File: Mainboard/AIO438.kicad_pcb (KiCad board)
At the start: 4 copper layers, 121 x 60 mm, 163 parts, among them J1 JST-PH 01x03, J10 U.FL, J11 JST-PH 01x02, J2 JST-PH 01x10, J3 PinHeader 02x03, J4 5mm screwterminal 01x12, J5 JST-PH 01x02, J6 JST-PH 01x02, J7 PinHeader 01x06, J8 USB_B_Micro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

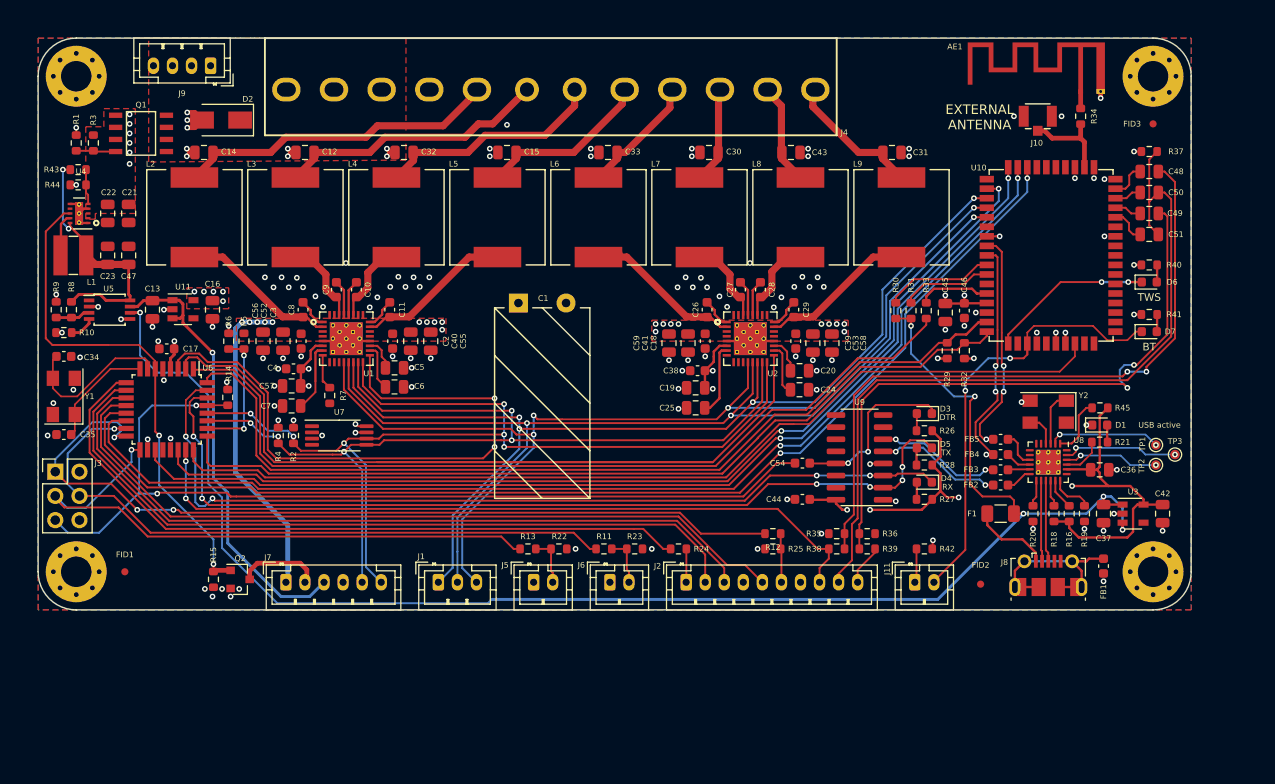
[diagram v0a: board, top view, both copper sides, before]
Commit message: Modify library references
As described in the README of the newly added libraries submodule.
Schematic and PCB are synced.

Hardware folder is renamed to mainboard
Any other PCBs can be put in their own subfolder in the gitrepo

Commit also swaps source/drain of Q1 because it appeared wrong for some
reason after updating all symbol/footprints.
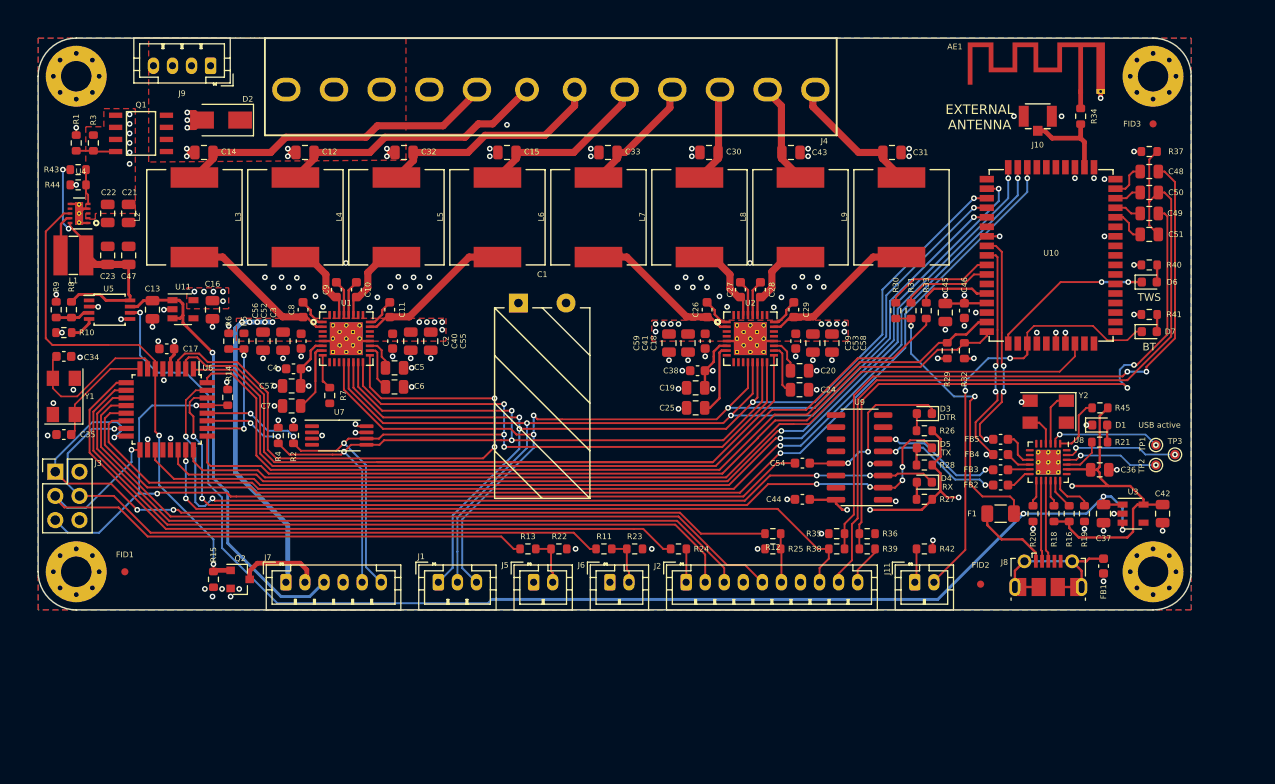
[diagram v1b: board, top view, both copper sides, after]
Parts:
- C1: footprint ZOUDIOfootprints:Cap_Rad_D10_P5_horizontal -> ZOUDIO-footprints:Cap_Rad_D10_P5_horizontal
- J10: footprint ZOUDIOfootprints:Hirose_U.FL-R-SMT-1 -> ZOUDIO-footprints:Hirose_U.FL-R-SMT-1
- J4: footprint ZOUDIOfootprints:Multicomp_12P_5mm -> ZOUDIO-footprints:Multicomp_12P_5mm
- L1: footprint ZOUDIOfootprints:SRN4012TA -> ZOUDIO-footprints:SRN4012TA
- L2, L3, L4, L5, L6, L7, L8, L9: footprint ZOUDIOfootprints:Murata_1274AS-H-100M -> ZOUDIO-footprints:Murata_1274AS-H-100M
- LOGO1: footprint ZOUDIOfootprints:ZOUDIO25mm -> ZOUDIO-footprints:ZOUDIO25mm
- Q1: footprint ZOUDIOfootprints:SOIC8_mosfet -> ZOUDIO-footprints:SOIC8_mosfet
- U1, U2: footprint ZOUDIOfootprints:TAS5825M -> ZOUDIO-footprints:TAS5825M
- U10: footprint ZOUDIOfootprints:BTM331 -> ZOUDIO-footprints:BTM331

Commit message: Add USB-C
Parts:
- removed J8: USB_B_Micro, Connector_USB:USB_Micro-B_Molex-105017-0001
- added P1: USB_C_Plug_USB2.0, Connector_USB:USB_C_Receptacle_Palconn_UTC16-G, F.Cu at (208.7, 128.0)

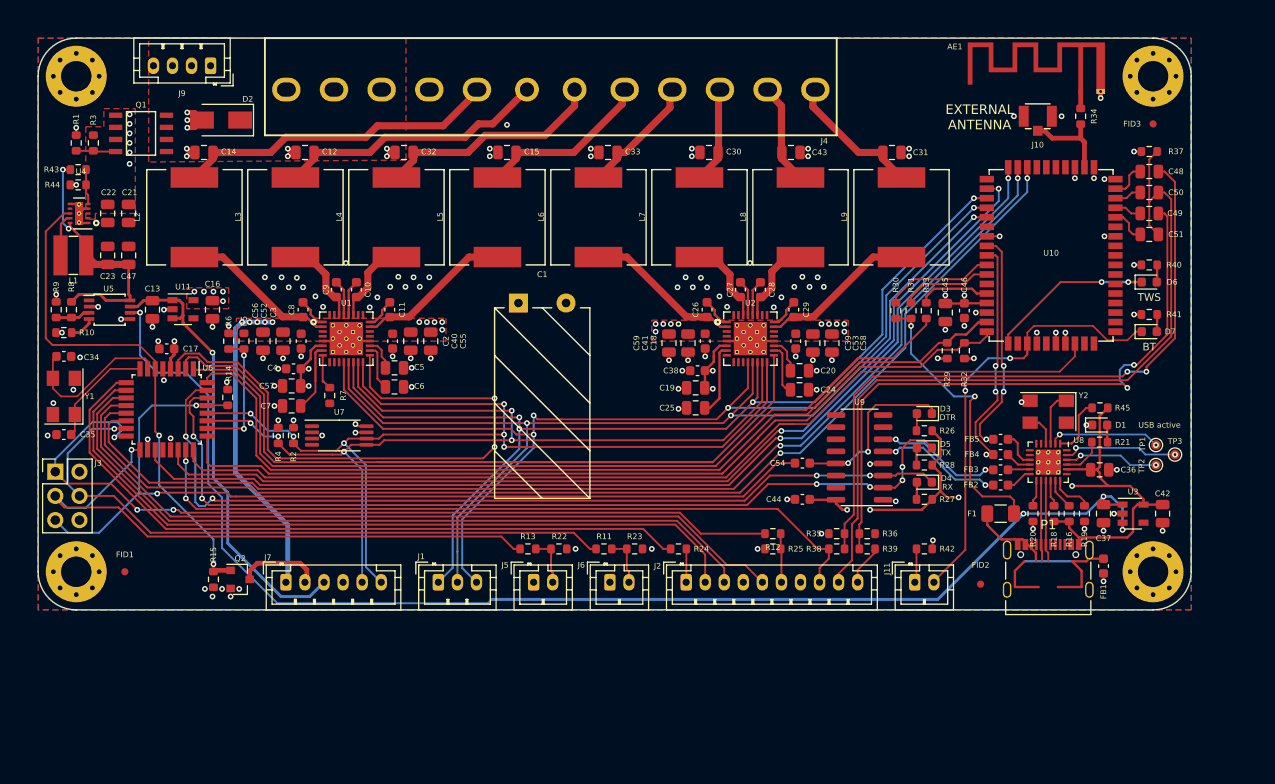
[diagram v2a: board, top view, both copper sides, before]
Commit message: Before testing CH340B and VCHG
Cleaned up amp lay-out a bit in the meanwhile
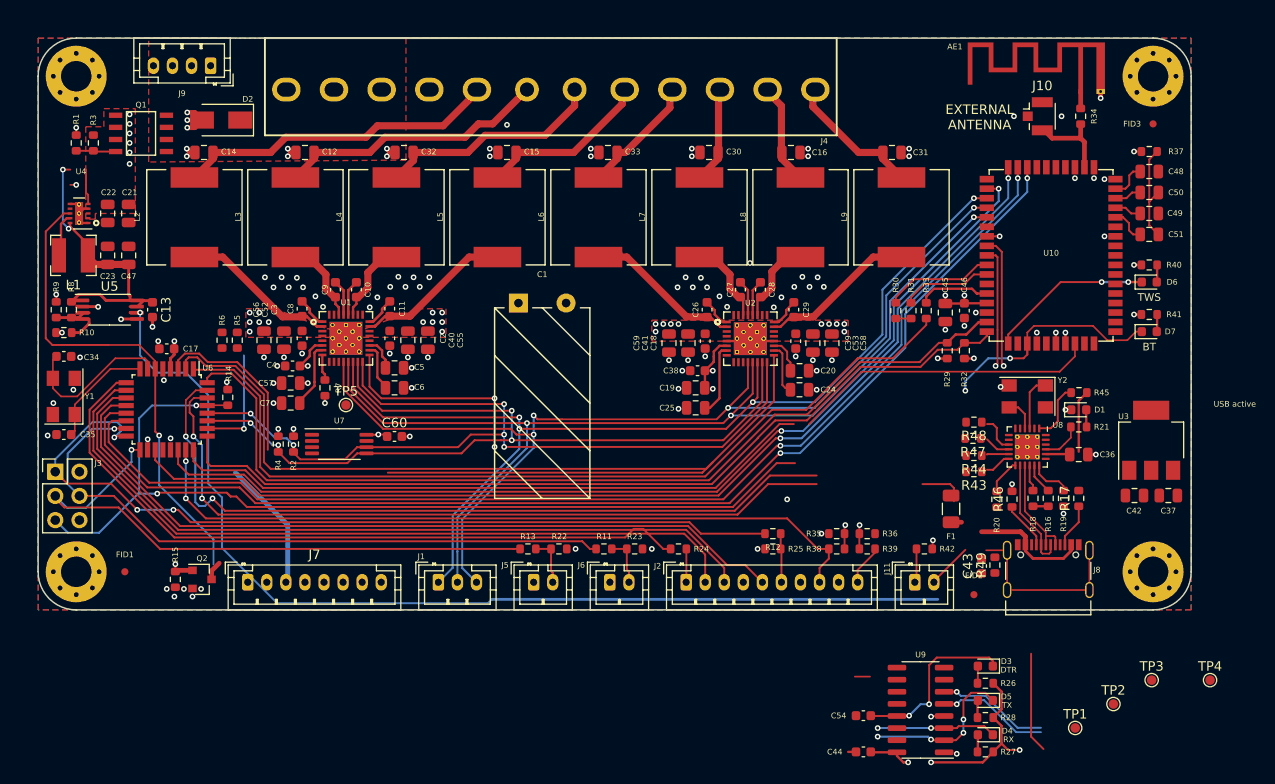
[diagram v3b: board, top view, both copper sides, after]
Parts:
- removed the C16 at (121.0, 100.8)
- removed FB1, FB2, FB3, FB4, FB5: 120R, Capacitor_SMD:C_0603_1608Metric
- removed P1: USB_C_Plug_USB2.0, Connector_USB:USB_C_Receptacle_Palconn_UTC16-G
- removed U11: LP5907MFX-3.3, Package_TO_SOT_SMD:SOT-23-5
- added C43: 100n, Capacitor_SMD:C_0603_1608Metric, F.Cu at (201.7, 127.7)
- added C60: 100n, Capacitor_SMD:C_0603_1608Metric, F.Cu at (140.1, 114.1)
- added J8: USB-C, Connector_USB:USB_C_Receptacle_Palconn_UTC16-G, F.Cu at (208.7, 128.0)
- added R17: 5k1, Resistor_SMD:R_0603_1608Metric, F.Cu at (211.9, 120.6)
- added R46: 5k1, Resistor_SMD:R_0603_1608Metric, F.Cu at (204.9, 120.7)
- added R47: 0R, Resistor_SMD:R_0603_1608Metric, F.Cu at (200.8, 114.3)
- added R48: 0R, Resistor_SMD:R_0603_1608Metric, F.Cu at (200.9, 112.6)
- added R49: 100k, Resistor_SMD:R_0603_1608Metric, F.Cu at (203.1, 127.6)
- added TP4: TestPoint, TestPoint:TestPoint_Pad_D1.0mm, F.Cu at (225.7, 139.7)
- added TP5: TestPoint, TestPoint:TestPoint_Pad_D1.0mm, F.Cu at (135.0, 110.8)
- C13: value 1u -> 100n; footprint Capacitor_SMD:C_0805_2012Metric -> Capacitor_SMD:C_0603_1608Metric
- C19: value 1u -> 4.7u
- H1, H2, H3, H4: value MountingHole -> Mounting hole
- J10: footprint ZOUDIO-footprints:Hirose_U.FL-R-SMT-1 -> Connector_Coaxial:U.FL_Hirose_U.FL-R-SMT-1_Vertical
- J7: value PinHeader 01x06 -> JST-PH 01x08; footprint Connector_JST:JST_PH_B6B-PH-K_1x06_P2.00mm_Vertical -> Connector_JST:JST_PH_B8B-PH-K_1x08_P2.00mm_Vertical
- L1: footprint ZOUDIO-footprints:SRN4012TA -> Inductor_SMD:L_Bourns-SRN4018
- R10: value 1K -> 1k
- R16, R18: value 100k -> 10k
- R2, R4: value 10k -> 1k
- R21: value 1k -> 10k
- R43: value 525k -> 0R
- R44: value 100k -> 0R
- R8: value 10k -> 100k
- R9: value 100k -> 36k
- U3: value LP5907MFX-3.3 -> AMS1117-3.3; footprint Package_TO_SOT_SMD:SOT-23-5 -> Package_TO_SOT_SMD:SOT-223-3_TabPin2
- U4: value TPS62175DQC -> TPS62177DQC
- U5: value TPS2113A -> TPS2111; footprint Package_SO:TSSOP-8_3x3mm_P0.65mm -> Package_SO:TSSOP-8_4.4x3mm_P0.65mm
- moved R43 99.2 mm to (200.9, 117.8), turned to 180 degrees
- moved R44 98.2 mm to (200.9, 116.1)
- moved TP1 30.9 mm to (211.5, 144.7)
- moved D5 27.3 mm to (202.1, 141.8)
- moved U9 27.3 mm to (195.3, 142.8)
- moved C54 27.3 mm to (189.3, 143.4)
- moved D4 27.3 mm to (202.1, 145.4)
- moved R26 27.3 mm to (202.1, 140.0)
- moved R28 27.3 mm to (202.1, 143.6)
- moved C44 27.3 mm to (189.3, 147.2)
- moved D3 27.3 mm to (202.1, 138.2)
- moved R27 27.3 mm to (202.1, 147.2)
- moved TP2 25.5 mm to (215.5, 142.2)
- moved TP3 23.8 mm to (219.6, 139.7)
- moved U3 7.93 mm to (219.5, 114.5), turned to 90 degrees
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- renumbered C43 to C16
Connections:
- net Net-(R7-Pad1) renamed /Amplifiers/Amplifier 1/ADR
- C13 pad 1: +5V -> GND
- C13 pad 2: GND -> /Power/3V3_buck
- C23 pad 1: /Power/5V_buck -> /Power/3V3_buck
- C36 pad 2: /USB/3V3 -> 3V3_USB
- C37 pad 1: 5V_usb -> 5V_USB
- C42 pad 1: /USB/3V3 -> 3V3_USB
- C44 pad 2: /USB/3V3 -> 3V3_USB
- C47 pad 1: /Power/5V_buck -> /Power/3V3_buck
- C48 pad 1: Net-(C48-Pad1) -> /User controls/AUX_L
- C49 pad 1: Net-(C49-Pad1) -> /User controls/AUX_R
- F1 pad 1: 5V_usb -> 5V_USB
- J10 pad 1: GND -> Net-(J10-Pad1)
- J10 pad 2: Net-(J10-Pad2) -> GND
- J2 pad 10: /User controls/AUX_R -> Net-(J2-Pad10)
- J2 pad 8: /User controls/AUX_L -> Net-(J2-Pad8)
- J7 pad 3: +5V -> +3V3
- J7 pad 4: +3V3 -> /Amplifiers/I2C_SDA
- J7 pad 5: /Amplifiers/I2C_SDA -> /Amplifiers/I2C_SCL
- J7 pad 6: /Amplifiers/I2C_SCL -> /Microcontroller/DTR
- L1 pad 2: /Power/5V_buck -> /Power/3V3_buck
- R10 pad 1: Net-(R10-Pad1) -> GND
- R10 pad 2: GND -> Net-(R10-Pad2)
- R16 pad 1: /USB/3V3 -> 3V3_USB
- R18 pad 1: /USB/3V3 -> 3V3_USB
- R26 pad 1: /USB/3V3 -> 3V3_USB
- R27 pad 1: /USB/3V3 -> 3V3_USB
- R28 pad 1: /USB/3V3 -> 3V3_USB
- R30 pad 2: 5V_usb -> 5V_USB
- R31 pad 2: 5V_usb -> 5V_USB
- R34 pad 1: Net-(J10-Pad2) -> Net-(J10-Pad1)
- R35 pad 1: GND -> /User controls/AUX_L
- R35 pad 2: Net-(C48-Pad1) -> Net-(J2-Pad8)
- R36 pad 1: GND -> /User controls/AUX_R
- R36 pad 2: Net-(C49-Pad1) -> Net-(J2-Pad10)
- R38 pad 1: /User controls/AUX_L -> GND
- R38 pad 2: Net-(C48-Pad1) -> /User controls/AUX_L
- R39 pad 1: /User controls/AUX_R -> GND
- R39 pad 2: Net-(C49-Pad1) -> /User controls/AUX_R
- R43 pad 1: /Power/5V_buck -> Net-(R43-Pad1)
- R43 pad 2: Net-(R43-Pad2) -> /USB/D1+
- R44 pad 1: Net-(R43-Pad2) -> Net-(R44-Pad1)
- R44 pad 2: GND -> /USB/D1-
- R45 pad 1: /USB/3V3 -> 3V3_USB
- R8 pad 2: /Power/5V_buck -> /Power/3V3_buck
- U10 pad 46: Net-(J10-Pad2) -> Net-(J10-Pad1)
- U3 pad 1: 5V_usb -> GND
- U3 pad 2: GND -> 3V3_USB
- U3 pad 3: 5V_usb -> 5V_USB
- U4 pad 10: /Power/5V_buck -> /Power/3V3_buck
- U4 pad 5: Net-(R43-Pad2) -> GND
- U5 pad 4: Net-(R10-Pad1) -> Net-(R10-Pad2)
- U5 pad 6: 5V_usb -> 3V3_USB
- U5 pad 7: +5V -> +3V3
- U5 pad 8: /Power/5V_buck -> /Power/3V3_buck
- U8 pad 11: Net-(FB3-Pad2) -> Net-(R44-Pad1)
- U8 pad 12: Net-(FB2-Pad2) -> Net-(R43-Pad1)
- U8 pad 14: Net-(J8-Pad2) -> /USB/D-
- U8 pad 15: Net-(J8-Pad3) -> /USB/D+
- U8 pad 20: /USB/3V3 -> 3V3_USB
- U9 pad 16: /USB/3V3 -> 3V3_USB
- U9 pad 4: /USB/3V3 -> 3V3_USB
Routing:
- net 5V_usb: track 170.0 -> 0.00 mm, vias 6 -> 0
- net 3V3_USB: track 0.00 -> 151.1 mm, vias 0 -> 5
- net /USB/3V3: track 80.4 -> 0.00 mm, vias 5 -> 0
- net /User controls/AUX_GND: track 82.5 -> 10.8 mm
- net Net-(C48-Pad1): track 71.6 -> 2.53 mm, vias 2 -> 1
- net Net-(C49-Pad1): track 66.6 -> 2.51 mm, vias 2 -> 1
- net +5V: track 47.3 -> 2.61 mm, vias 1 -> 0
- net VDD: track 34.9 -> 0.83 mm, vias 26 -> 28
- net /Amplifiers/AMP1_PDN: track 65.0 -> 40.4 mm
- net Net-(FB1-Pad2): track 19.6 -> 0.00 mm
- net Net-(C43-Pad2): track 0.00 -> 19.2 mm
- net 5V_USB: track 0.00 -> 17.0 mm
- net /Bluetooth/LED5: track 45.6 -> 28.9 mm
- net /Amplifiers/I2C_SCL: track 106.7 -> 91.3 mm, vias 6 -> 5
- net /Amplifiers/I2C_SDA: track 103.9 -> 90.2 mm, vias 5 -> 4
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- removed copper zone on F.Cu, net +3V3

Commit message: Result after weekend of lay-out
Pretty far, just neats to be cleaned up for production.
Does not pass DRC yet.
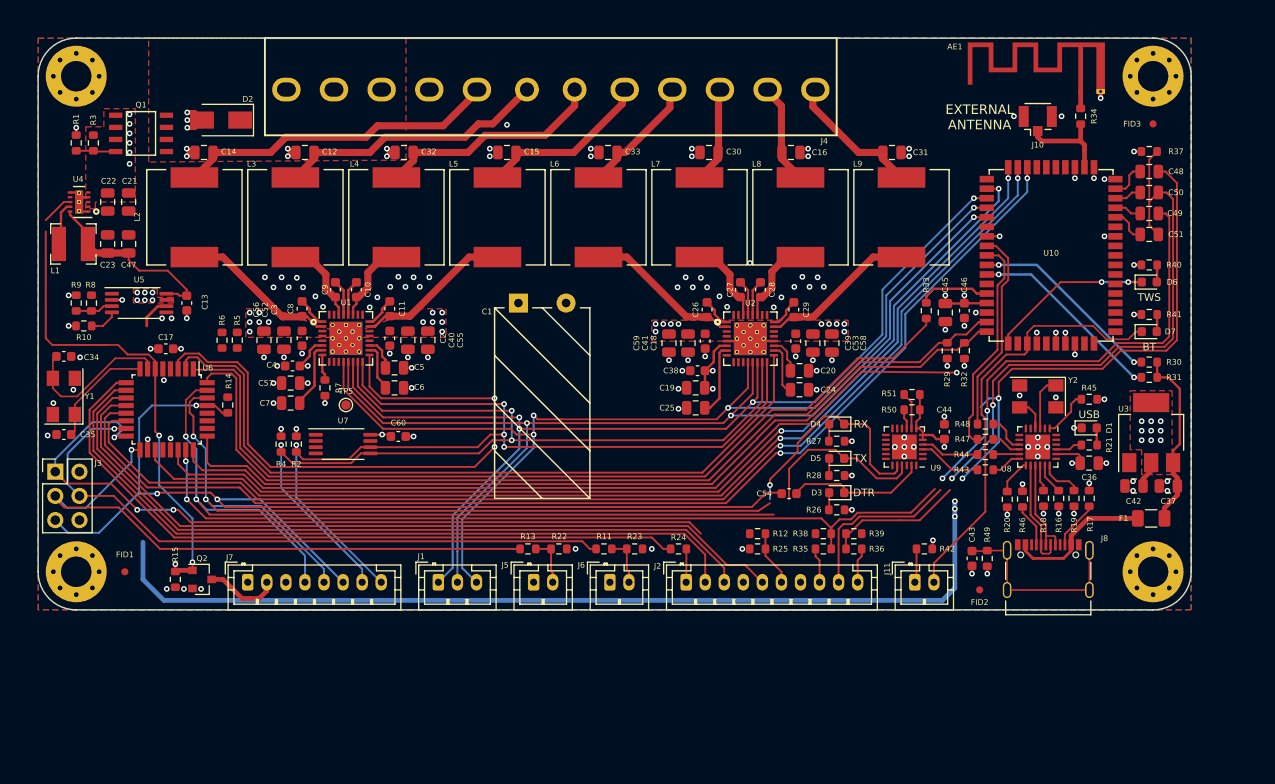
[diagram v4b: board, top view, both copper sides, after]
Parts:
- removed J9: JST-PH 01x04, Connector_JST:JST_PH_B4B-PH-K_1x04_P2.00mm_Vertical
- removed TP1, TP2, TP3, TP4: TestPoint, TestPoint:TestPoint_Pad_D1.0mm
- added R50: 1k, Resistor_SMD:R_0603_1608Metric, F.Cu at (194.4, 111.3)
- added R51: 10k, Resistor_SMD:R_0603_1608Metric, F.Cu at (194.4, 109.7)
- U8: footprint Package_DFN_QFN:QFN-24-1EP_4x4mm_P0.5mm_EP2.6x2.6mm_ThermalVias -> Package_DFN_QFN:QFN-24-1EP_4x4mm_P0.5mm_EP2.6x2.6mm
- U9: value CH340B -> CP2102N; footprint Package_SO:SOIC-16_3.9x9.9mm_P1.27mm -> Package_DFN_QFN:QFN-24-1EP_4x4mm_P0.5mm_EP2.6x2.6mm
- moved D4 36.1 mm to (186.5, 112.8)
- moved R27 36.1 mm to (186.5, 114.6)
- moved C44 34.7 mm to (197.8, 113.6), turned to 270 degrees
- moved D5 29.8 mm to (186.5, 116.4)
- moved R28 29.8 mm to (186.5, 118.2)
- moved U9 27.7 mm to (193.6, 115.2)
- moved R30 27.1 mm to (219.3, 106.3), turned to 0 degrees
- moved R31 26.0 mm to (219.3, 107.9), turned to 0 degrees
- moved C54 24.6 mm to (181.5, 120.1)
- moved R26 24.0 mm to (186.5, 121.8)
- moved D3 24.0 mm to (186.5, 120.0)
- moved F1 21.0 mm to (219.5, 122.7), turned to 180 degrees
- moved C13 3.67 mm to (118.3, 100.1), turned to 90 degrees
- moved U5 3.18 mm to (113.3, 100.1)
- moved R9 2.21 mm to (106.7, 100.1)
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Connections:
- J7 pad 4: /Amplifiers/I2C_SDA -> /USB to UART/UART_RX
- J7 pad 5: /Amplifiers/I2C_SCL -> /Microcontroller/UART_RX
- J7 pad 6: /Microcontroller/DTR -> /Microcontroller/RESET
- J7 pad 7: /Microcontroller/UART_RX -> /Amplifiers/I2C_SDA
- J7 pad 8: /USB to UART/UART_RX -> /Amplifiers/I2C_SCL
- R43 pad 2: /USB/D1+ -> /USB to UART/D+
- R44 pad 2: /USB/D1- -> /USB to UART/D-
- U9 pad 1: GND -> Net-(U9-Pad1)
- U9 pad 13: /Microcontroller/DTR -> Net-(U9-Pad13)
- U9 pad 16: 3V3_USB -> Net-(U9-Pad16)
- U9 pad 2: /Microcontroller/UART_RX -> GND
- U9 pad 3: /USB to UART/UART_RX -> /USB to UART/D+
- U9 pad 4: 3V3_USB -> /USB to UART/D-
- U9 pad 5: /USB/D1+ -> 3V3_USB
- U9 pad 6: /USB/D1- -> 3V3_USB
- U9 pad 7: Net-(U9-Pad7) -> 3V3_USB
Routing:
- net /User controls/AUX_GND: track 10.8 -> 78.0 mm, vias 0 -> 2
- net /User controls/AUX_L: track 78.8 -> 143.0 mm, vias 2 -> 4
- net /User controls/AUX_R: track 4.26 -> 61.5 mm, vias 0 -> 2
- net /Amplifiers/AMP2_PDN: track 114.1 -> 80.1 mm
- net 3V3_USB: track 151.1 -> 123.4 mm, vias 5 -> 20
- net /Power/5V_buck: track 27.3 -> 0.00 mm, vias 2 -> 0
- net /Amplifiers/AMP1_PDN: track 40.4 -> 67.6 mm
- net /USB to UART/UART_RX: track 94.1 -> 115.5 mm, vias 4 -> 3
- net /Power/3V3_buck: track 0.85 -> 20.2 mm, vias 1 -> 0
- net +3V3: track 49.9 -> 32.7 mm, vias 20 -> 25
- net /Bluetooth/LED5: track 28.9 -> 44.9 mm, vias 2 -> 0
- net /Microcontroller/RESET: track 100.9 -> 114.7 mm, vias 2 -> 3
- net /Microcontroller/PC1: track 101.9 -> 88.7 mm, vias 0 -> 2
- net /Microcontroller/UART_RX: track 95.8 -> 107.9 mm, vias 6 -> 2
- net /USB/D1+: track 11.7 -> 0.00 mm, vias 1 -> 0
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- added copper zone on F.Cu, net +3V3
- added copper zone on F.Cu, net 3V3_USB
- added copper zone on In2.PWR, net 3V3_USB
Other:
- board text added: "USB"
- board text removed: "USB active"
